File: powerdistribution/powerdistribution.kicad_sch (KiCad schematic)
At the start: 126 parts, among them IC1 NCP718ASNADJT1G, J1 282837-2, J2 282837-2, J3 M20-6102045, Q1 IRLML0030, Q2 IRLML0030, Q3 IRLML0030, Q5 IRLML0030, U1 BQ7790512PW, U2 AP64501QSP-13, U3 AP64501QSP-13, U4 AP64501QSP-13, U5 TPS1HC30BQPWPRQ1, U6 TPS1HC30BQPWPRQ1, U7 ESP32-DEVKIT-V1, U8 LD1117S50TR_SOT223, U9 MIC29302AWD-TR

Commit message: updated pyro
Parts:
- R40, R41: value 10k -> 20k
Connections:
- net GND: now also Q3.2 (S), Q5.2 (S); no longer Q3.3 (D), Q5.3 (D)
- net PYRO2CONN: now reaches R41.1
- net PYRO2CONN: now also R43.1
- net at J2.2, R41.2: now also Q3.3 (D); no longer Q3.2 (S), R43.1
- net at J1.2, R40.2: now also Q5.3 (D); no longer Q5.2 (S), R42.1
- net PYRO1CONN: now reaches R40.1
- net PYRO1CONN: now also R42.1
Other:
- moved on the sheet: J1, J2, Q3, Q5, R35, R36, R40, R41, R42, R43

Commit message: dnp 12v buck, some notes
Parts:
- added C44, C45: 220nf, Capacitor_SMD:C_0603_1608Metric_Pad1.08x0.95mm_HandSolder, symbol Device:C_Small
- added J6: Conn_01x02, Connector_PinHeader_2.54mm:PinHeader_1x02_P2.54mm_Vertical, symbol Connector_Generic:Conn_01x02
- added M1, M2: Motor_Servo, Connector_PinHeader_2.54mm:PinHeader_1x03_P2.54mm_Vertical, symbol Motor:Motor_Servo
- added R56, R57, R58, R59: 10k, Resistor_SMD:R_0603_1608Metric_Pad0.98x0.95mm_HandSolder, symbol Device:R_US
- added R60, R61, R62, R63, R66: 5k, Resistor_SMD:R_0603_1608Metric_Pad0.98x0.95mm_HandSolder, symbol Device:R_US
- added R64: ~, Resistor_SMD:R_0603_1608Metric_Pad0.98x0.95mm_HandSolder, symbol Device:R_US
- added R65: 1k, Resistor_SMD:R_0603_1608Metric_Pad0.98x0.95mm_HandSolder, symbol Device:R_US
- added TP7, TP8: TestPoint, Connector_PinHeader_2.00mm:PinHeader_1x01_P2.00mm_Vertical, symbol Connector:TestPoint
- added U10: TPS1HC30BQPWPRQ1, HPRfootprints:IC_TPS1HC30BQPWPRQ1, symbol HPRlibrary:TPS1HC30BQPWPRQ1
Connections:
- net 6V: now also M1.2 (+), M2.2 (+); no longer C18.1, C19.1, C20.1, L2.1, R13.1
- net 6V_DIAGEN: now also R58.1, R59.2, R61.1, TP7.1
- net 6V_EN: now also R56.1, R57.2, R60.1, TP8.1
- net GND: now also C44.1, C45.1, J6.2 (Pin_2), M1.3 (-), M2.3 (-), R57.1, R59.1, R62.1, R64.2, R65.1, U10.1 (GND), U10.15 (EXP)
- net LDO_5V: now also R56.2, R58.2
- net Pack+: now also C44.2, J6.1 (Pin_1), U10.12 (VBB), U10.13 (VBB__1)
- net at C11.2, C5.2, U3.2 (VIN)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: now also U10.10 (VOUT__1), U10.9 (VOUT)
- new net: R63.1, U10.4 (~{FAULT})
- new net: R64.1, U10.7 (ILIM)
- new net: R62.2, U10.5 (LATCH)
- new net: R65.2, R66.1, U10.6 (SNS)
- new net: R60.2, U10.2 (EN)
- new net: R61.2, U10.3 (DIAG_EN)
- new net 12V: C18.1, C19.1, C20.1, L2.1, R13.1
- new net 12v_cursns: C45.2, R66.2
- new net 12v_fault: R63.2
- new net servo1_pwm: M1.1 (PWM)
- new net servo2_pwm: M2.1 (PWM)
- no-connect marks 6 -> 9
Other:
- note added: "Camera"
- note added: "External Batt"
- note added: "I don't think ESP32 doesn't need to be on before pin is pulled though"
- note added: "Other Headers/Ports"
- note added: "Pin Switch Screw Footprints (smthg like FIT0586)"
- note added: "Sensor SPI and other serial lines can be placed on connector to esp if needed"
- note added: "__V Buck"
- note removed: "3.3V Buck [DNP]"
- note removed: "Headers and Ports"
- note removed: "PIN SWITCH TO ENABLE"
- moved on the sheet: C42, C43, IC1, R54, R55

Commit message: update bms parts + board size
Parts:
- removed C1, C2, C3, C4: C0603C104K5RACTU, HPRfootprints:CAPC1608X90, symbol HPRsymbols:C0603C104K5RACTU
- removed C37, C38: UMK107AB7105KA-T, HPRfootprints:CAPC1608X95N, symbol HPRsymbols:UMK107AB7105KA-T
- removed J3: M20-6102045, HPRfootprints:RHDR40W66P254_2X20_5146X500X1105P, symbol HPRlibrary:M20-6102045
- removed R15, R17: ERJ2RKF1004X, HPRfootprints:RES_ERJ2RKF1004X, symbol HPRsymbols:ERJ2RKF1004X
- removed R16, R6: R_US, symbol Device:R_US
- removed R44: CSNL2512FT1L00, HPRfootprints:STA_CSNL25121_STP, symbol HPRsymbols:CSNL2512FT1L00
- removed R7: RC1206FR-074K53L, HPRfootprints:RC1206N_YAG, symbol HPRsymbols:RC1206FR-074K53L
- removed R8: RC0603FR-0710KL, HPRfootprints:RESC1607X60N, symbol HPRsymbols:RC0603FR-0710KL
- added C1, C2, C3, C4: 0.1μF, Capacitor_SMD:C_0603_1608Metric_Pad1.08x0.95mm_HandSolder, symbol Device:C_Small
- added C37, C38: C_Small, Capacitor_SMD:C_0603_1608Metric_Pad1.08x0.95mm_HandSolder, symbol Device:C_Small
- added J3: ESQ-113-12-G-D, HPRfootprints:SAMTEC_ESQ-113-12-G-D, symbol HPRsymbols:ESQ-113-12-G-D
- added R15, R16, R17, R6, R67, R7, R8: R_Small, Resistor_SMD:R_0603_1608Metric_Pad0.98x0.95mm_HandSolder, symbol Device:R_Small
- R1, R2, R3, R4, R5: footprint HPRfootprints:R0402 -> Resistor_SMD:R_0603_1608Metric_Pad0.98x0.95mm_HandSolder
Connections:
- net AVdd: no longer U1.2 (AVDD)
- net GND: now also C1.2, C2.2, C3.2, C37.2, C38.2, C4.1, R16.2, R17.1, R6.1
- net Vdd: no longer U1.1 (VDD)
- net sns-: now also R17.2, R67.2
- net at R4.2, U1.3 (VC5), U1.4 (VC4): now also C4.2
- net at Q2.1 (G): now also R15.2, R16.1
- net at Q1.1 (G): now also R67.1, R7.2
- net at RT1.1, U1.15 (TS): now also R8.2
- net at U1.11 (DSG): now also R7.1
- net at U1.13 (CHG): now also R15.1
- net at U1.14 (LD): now also R6.2
- net at U1.16 (VTB): now also R8.1
- net at R3.2, U1.5 (VC3): now also C3.1
- net at R2.2, U1.6 (VC2): now also C2.1
- net at R1.2, U1.7 (VC1): now also C1.1
- new net: C37.1, U1.2 (AVDD)
- new net: C38.1, U1.1 (VDD)

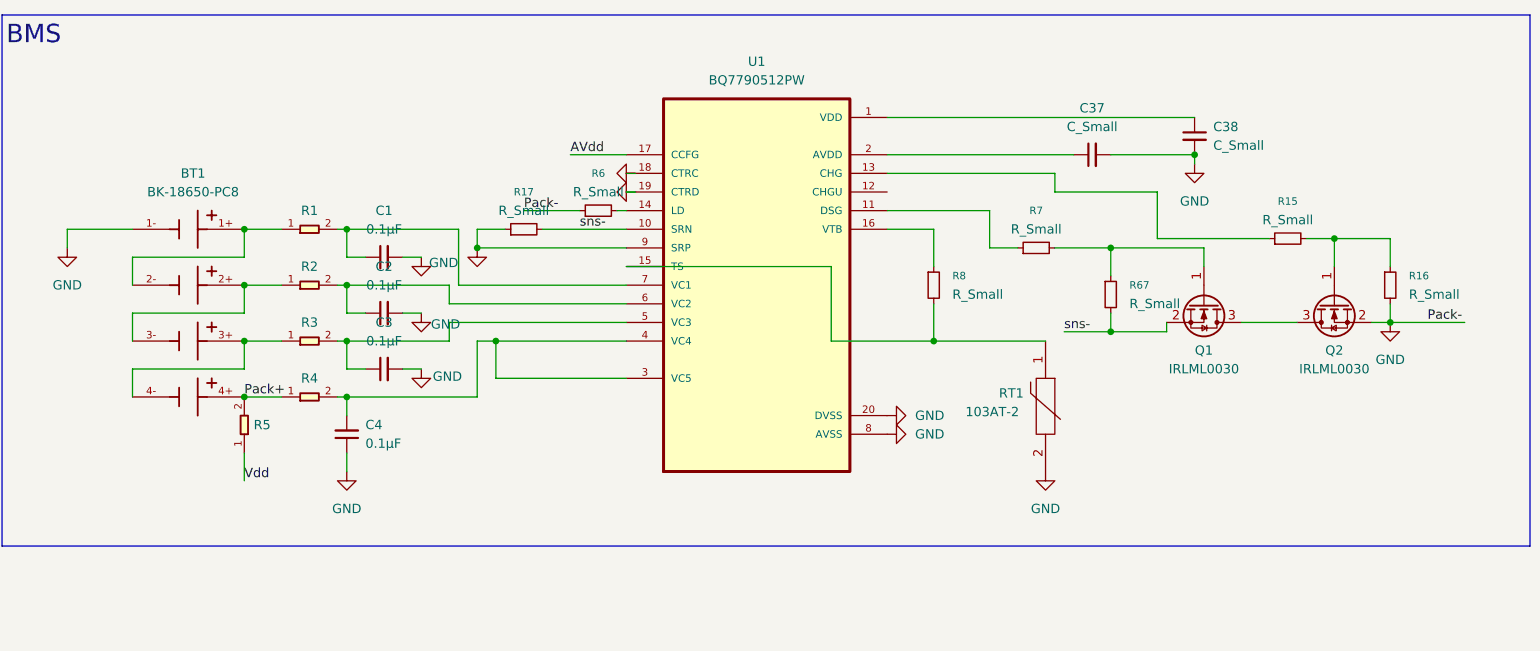
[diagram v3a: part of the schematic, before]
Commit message: update bms to 3 battery
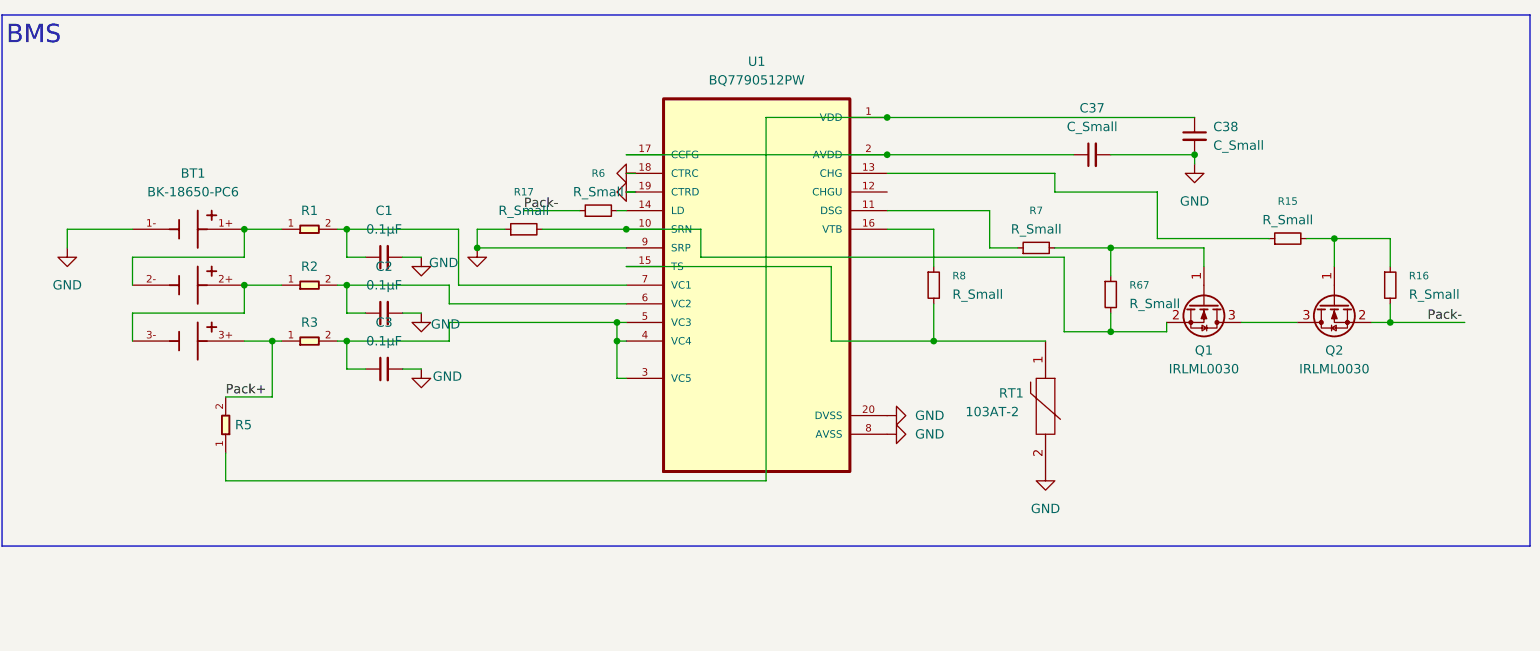
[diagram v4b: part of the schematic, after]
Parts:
- removed BT1: BK-18650-PC8, HPRfootprints:BAT_BK-18650-PC8, symbol HPRsymbols:BK-18650-PC8
- removed C4: 0.1μF, Capacitor_SMD:C_0603_1608Metric_Pad1.08x0.95mm_HandSolder, symbol Device:C_Small
- removed R4: 1K, Resistor_SMD:R_0603_1608Metric_Pad0.98x0.95mm_HandSolder, symbol HPRsymbols:SMD-RES-1K-5_-1_16W_0402_
- added BT1: BK-18650-PC6, HPRfootprints:BAT_BK-18650-PC6, symbol HPRsymbols:BK-18650-PC6
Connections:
- net AVdd is gone; now on an unnamed net: U1.17 (CCFG)
- net Vdd is gone; now on an unnamed net: R5.1
- net GND: now also BT1.1-; no longer Q2.2 (S), R16.2, R6.1
- net Pack+: now also R3.1, BT1.3+
- net at U1.3 (VC5), U1.4 (VC4): now also C3.1, R3.2, U1.5 (VC3)
- net at R2.1: now also BT1.2+, BT1.3-
- net at R1.1: now also BT1.1+, BT1.2-
- net sns-: no longer names the net of Q1.2 (S), R17.2, R67.2, U1.10 (SRN)
- new net Pack-: Q2.2 (S), R16.2, R6.1
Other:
- moved on the sheet: R5

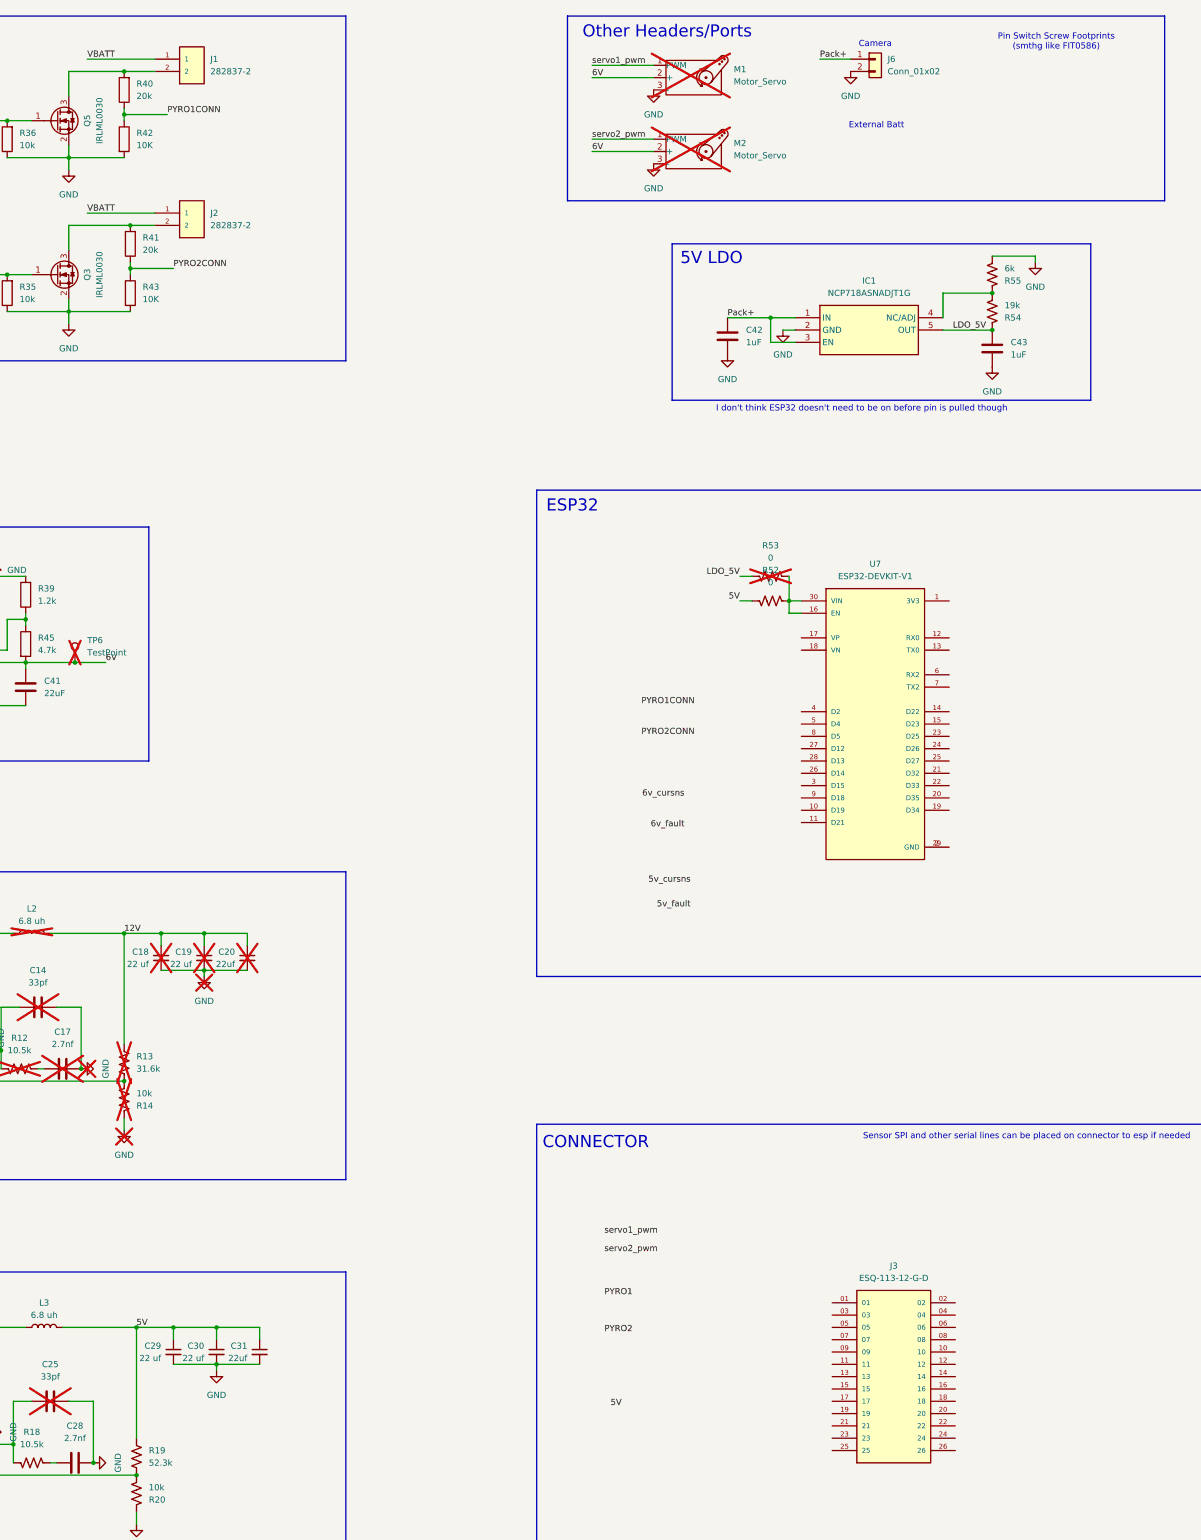
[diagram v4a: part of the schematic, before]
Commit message: new board size+routing
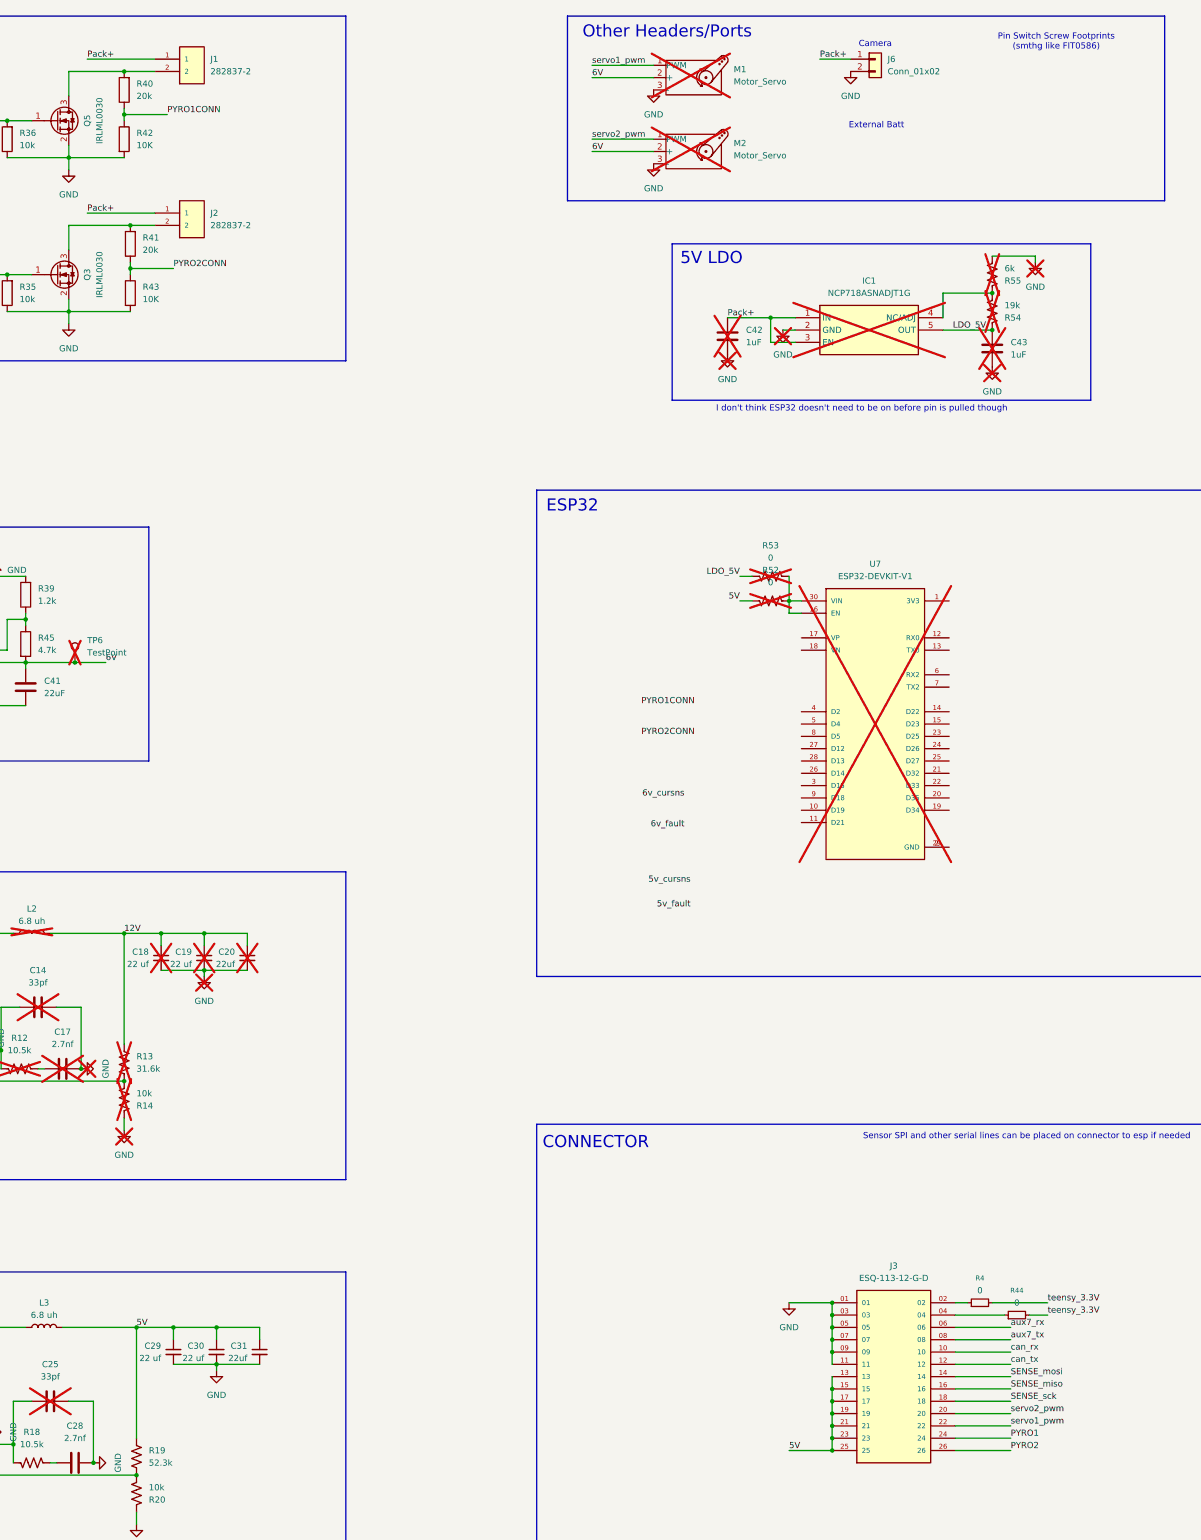
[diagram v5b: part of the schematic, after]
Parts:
- added R4, R44: 0, Resistor_SMD:R_0603_1608Metric_Pad0.98x0.95mm_HandSolder, symbol Device:R_Small
- C42, C43, IC1, R52, R54, R55, U7: now not fitted
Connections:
- net VBATT is gone; now on net Pack+: J1.1, J2.1
- net 5V: now also J3.13, J3.15, J3.17, J3.19, J3.21, J3.23, J3.25
- net GND: now also J3.01, J3.03, J3.05, J3.07, J3.09, J3.11
- net PYRO1: now also J3.24
- net PYRO2: now also J3.26
- net servo1_pwm: now also J3.22
- net servo2_pwm: now also J3.20
- net at J3.02: now also R4.1
- net at J3.04: now also R44.1
- net aux7_rx: now reaches J3.06
- net aux7_tx: now reaches J3.08
- net can_rx: now reaches J3.10
- net can_tx: now reaches J3.12
- net SENSE_mosi: now reaches J3.14
- net SENSE_miso: now reaches J3.16
- net SENSE_sck: now reaches J3.18
- new net teensy_3.3V: R4.2, R44.2

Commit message: pd placement
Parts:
- removed R4, R44: 0, Resistor_SMD:R_0603_1608Metric_Pad0.98x0.95mm_HandSolder, symbol Device:R_Small
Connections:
- net 5V: no longer J3.13, J3.15, J3.17, J3.19, J3.21, J3.23
- net 6V_DIAGEN: no longer R58.1, R59.2, R61.1, TP7.1
- net 6V_EN: no longer R56.1, R57.2, R60.1, TP8.1
- net GND: no longer J3.01, J3.03, J3.05, J3.07, J3.09, J3.11
- net PYRO1: no longer J3.24
- net PYRO2: no longer J3.26
- net SENSE_miso: no longer J3.16
- net SENSE_mosi: no longer J3.14
- net SENSE_sck: no longer J3.18
- net servo1_pwm: no longer J3.22
- net servo2_pwm: no longer J3.20
- net aux7_rx: no longer names the net of J3.06
- net aux7_tx: no longer names the net of J3.08
- net can_rx: no longer names the net of J3.10
- net can_tx: no longer names the net of J3.12
- new net 12V_DIAGEN: R58.1, R59.2, R61.1, TP7.1
- new net 12V_EN: R56.1, R57.2, R60.1, TP8.1

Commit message: starting new placement
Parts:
- C42, C43, IC1, R54, R55: now fitted
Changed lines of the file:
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@@
 		(exclude_from_sim no)
 		(in_bom yes)
-		(on_board no)
-		(dnp yes)
+		(on_board yes)
+		(dnp no)
 		(fields_autoplaced yes)
 		(property "Reference" "R55"
@@
 		(exclude_from_sim no)
 		(in_bom yes)
-		(on_board no)
-		(dnp yes)
+		(on_board yes)
+		(dnp no)
 		(fields_autoplaced yes)
 		(property "Reference" "#PWR051"
@@
 		(exclude_from_sim no)
 		(in_bom yes)
-		(on_board no)
-		(dnp yes)
+		(on_board yes)
+		(dnp no)
 		(fields_autoplaced yes)
 		(property "Reference" "R54"
@@
 		(exclude_from_sim no)
 		(in_bom yes)
-		(on_board no)
-		(dnp yes)
+		(on_board yes)
+		(dnp no)
 		(fields_autoplaced yes)
 		(property "Reference" "C43"
@@
 		(exclude_from_sim no)
 		(in_bom yes)
-		(on_board no)
-		(dnp yes)
+		(on_board yes)
+		(dnp no)
 		(fields_autoplaced yes)
 		(property "Reference" "IC1"
@@
 		(exclude_from_sim no)
 		(in_bom yes)
-		(on_board no)
-		(dnp yes)
+		(on_board yes)
+		(dnp no)
 		(fields_autoplaced yes)
 		(property "Reference" "#PWR049"
@@
 		(exclude_from_sim no)
 		(in_bom yes)
-		(on_board no)
-		(dnp yes)
+		(on_board yes)
+		(dnp no)
 		(fields_autoplaced yes)
 		(property "Reference" "#PWR048"
@@
 		(exclude_from_sim no)
 		(in_bom yes)
-		(on_board no)
-		(dnp yes)
+		(on_board yes)
+		(dnp no)
 		(fields_autoplaced yes)
 		(property "Reference" "C42"
@@
 		(exclude_from_sim no)
 		(in_bom yes)
-		(on_board no)
-		(dnp yes)
+		(on_board yes)
+		(dnp no)
 		(property "Reference" "#PWR052"
 			(at 520.7 93.98 0)
